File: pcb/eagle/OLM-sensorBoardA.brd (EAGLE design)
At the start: 91.9 x 57.1 mm, 19 parts, among them IC1 MAX31855, J1 1X2-3.5MM, J2 1X2-3.5MM, U1 AM2302

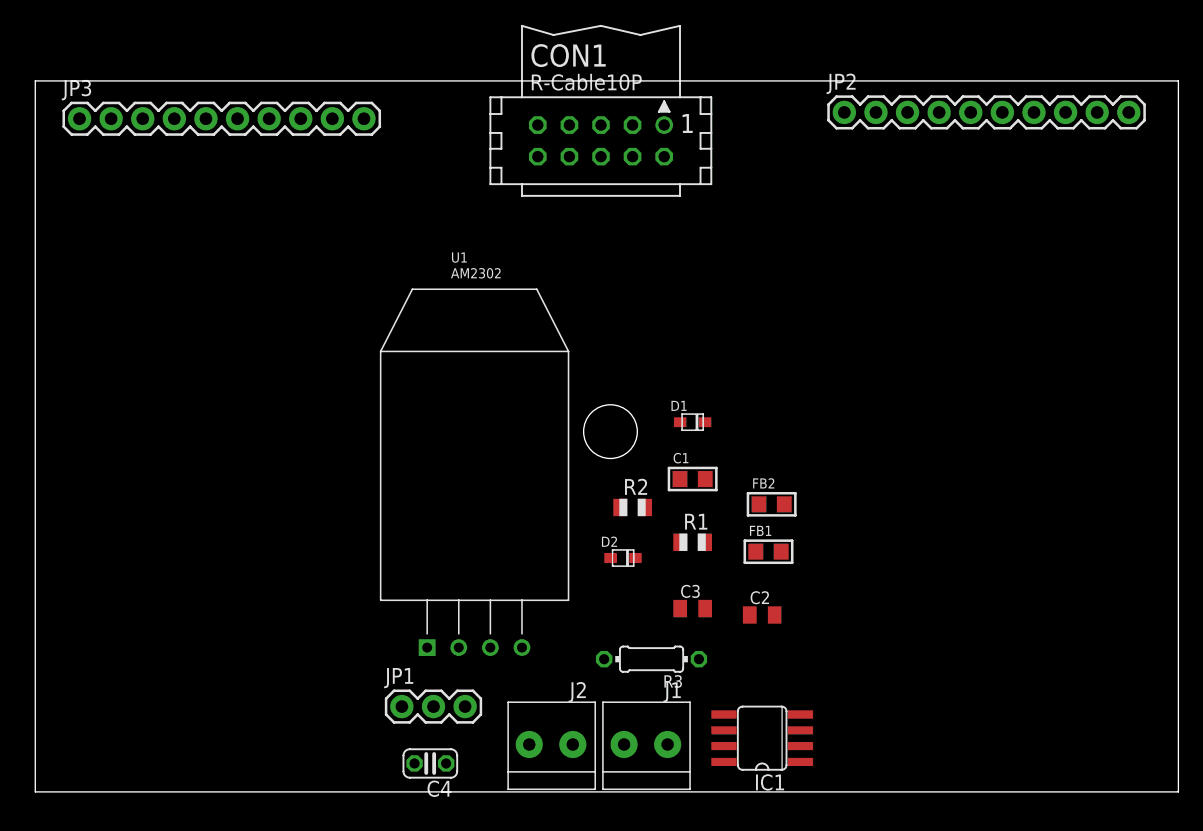
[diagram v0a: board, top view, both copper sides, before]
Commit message: made sensor board
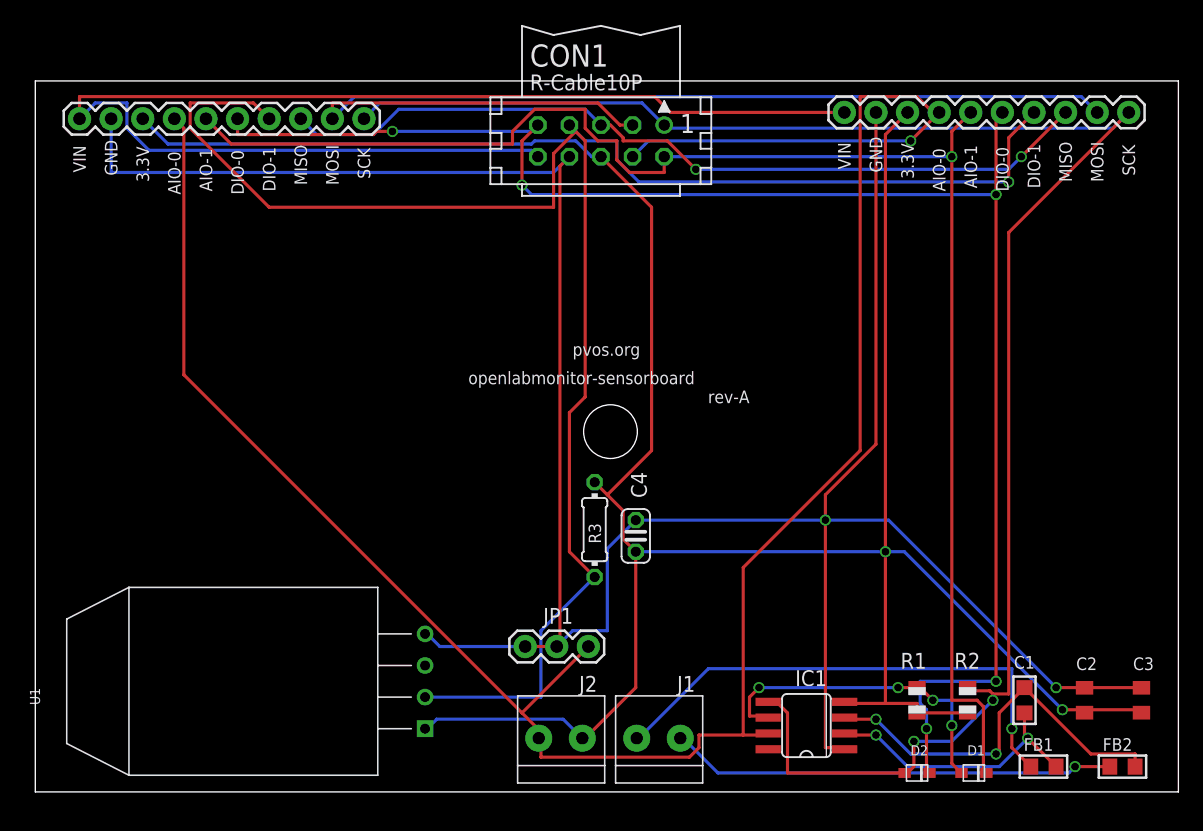
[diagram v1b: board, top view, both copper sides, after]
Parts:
- moved C3 36.8 mm to (88.9, 7.37), turned to 90 degrees
- moved D1 36.1 mm to (75.4, 1.52)
- moved FB2 35.2 mm to (87.4, 2.03)
- moved C1 32.1 mm to (79.5, 7.37), turned to 90 degrees
- moved R2 31.1 mm to (74.9, 7.37), turned to 90 degrees
- moved D2 29.3 mm to (70.9, 1.52)
- moved FB1 28.0 mm to (81.0, 2.03)
- moved C2 26.8 mm to (84.3, 7.37), turned to 90 degrees
- moved C4 24.6 mm to (48.3, 20.6), turned to 90 degrees
- moved U1 24.3 mm to (17.5, 8.89), turned to 90 degrees
- moved R1 22.1 mm to (70.9, 7.37), turned to 90 degrees
- moved R3 11.4 mm to (45.0, 21.1), turned to 270 degrees
- moved JP1 11.0 mm to (39.4, 11.7)
- moved IC1 3.70 mm to (62.0, 5.33)
- moved J1 1.14 mm to (50.0, 4.32)
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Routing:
- net +3V3: track 0.00 -> 211.4 mm, vias 0 -> 2
- net GND: track 0.00 -> 207.5 mm, vias 0 -> 2
- net AIO-0: track 0.00 -> 178.9 mm, vias 0 -> 1
- net DIO-1: track 0.00 -> 151.1 mm, vias 0 -> 1
- net SCK: track 0.00 -> 145.2 mm, vias 0 -> 2
- net DIO-0: track 0.00 -> 129.3 mm, vias 0 -> 5
- net AIO-1: track 0.00 -> 123.9 mm, vias 0 -> 1
- net VIN: track 0.00 -> 104.1 mm
- net MOSI: track 0.00 -> 88.9 mm
- net MISO: track 0.00 -> 66.9 mm, vias 0 -> 2
- net N$1: track 0.00 -> 41.0 mm, vias 0 -> 1
- net N$5: track 0.00 -> 35.9 mm, vias 0 -> 1
- net N$6: track 0.00 -> 31.8 mm, vias 0 -> 2
- net CS: track 0.00 -> 26.4 mm, vias 0 -> 4
- net N$4: track 0.00 -> 22.1 mm, vias 0 -> 2
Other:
- board text added: "3.3V"
- board text added: "AIO-0"
- board text added: "AIO-1"
- board text added: "DIO-0"
- board text added: "DIO-1"
- board text added: "GND"
- board text added: "MISO"
- board text added: "MOSI"
- board text added: "SCK"
- board text added: "VIN"
- board text added: "openlabmonitor-sensorboard"
- board text added: "pvos.org"
- board text added: "rev-A"
